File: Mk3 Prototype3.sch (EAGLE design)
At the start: 150 parts, among them IC1 TPD3E001DRL, IC2 TPS62082, IC3 STM32F401V, IC4 BQ24092, IC6 CC3100MOD, IC7 BQ2970, IC8 LSM6DS3, IC9 LIS3MDL, J1 ZX62-AB-5PA(11), J2 ER-CON50HT-1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

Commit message: updating usd
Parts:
- U1: value USD-SOCKET-SDIODM3AT_0011 -> USD-SOCKET-SDIO; device TiLDA Mk3 Parts:USD-SOCKET-SDIODM3AT_0011 -> TiLDA Mk3 Parts:USD-SOCKET-SDIO
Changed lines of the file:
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@@
 <part name="GND14" library="TiLDA Mk3 Parts" deviceset="GND" device=""/>
 <part name="R24" library="TiLDA Mk3 Parts" deviceset="R-EU_" device="0603K-SMALL" value="0603/330/5%"/>
-<part name="U1" library="TiLDA Mk3 Parts" deviceset="USD-SOCKET-SDIO" device="DM3AT_0011">
+<part name="U1" library="TiLDA Mk3 Parts" deviceset="USD-SOCKET-SDIO" device="" value="USD-SOCKET-SDIO">
 <attribute name="FARNELL" value="2427719"/>
 </part>

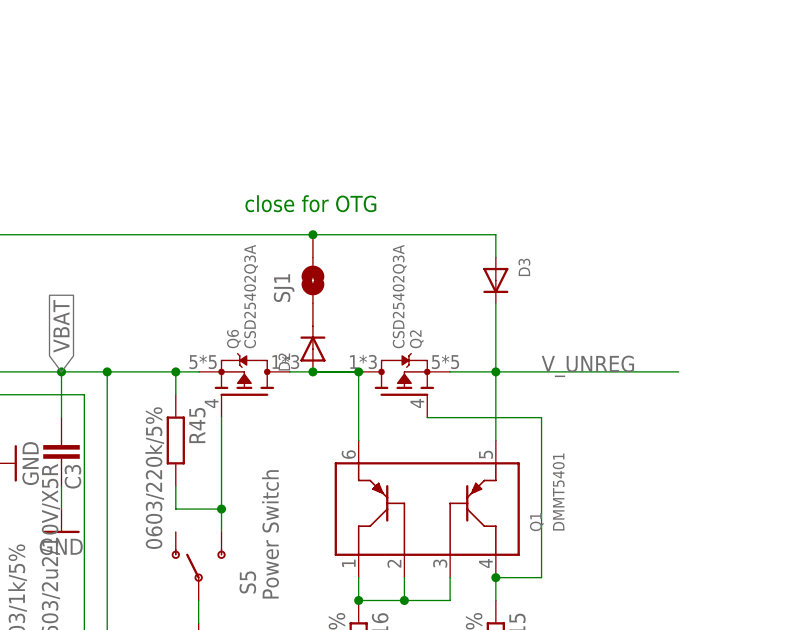
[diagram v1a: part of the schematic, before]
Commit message: changing out diodes
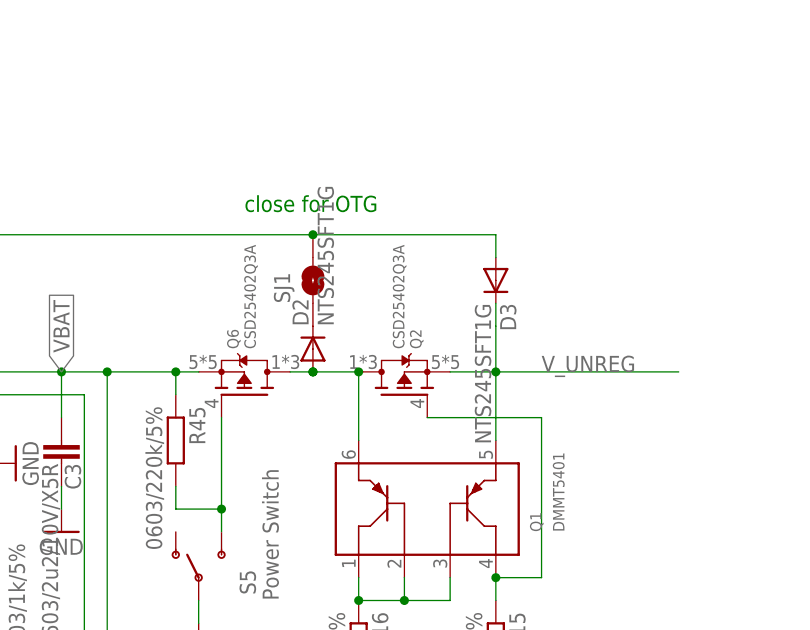
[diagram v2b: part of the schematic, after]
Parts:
- D2, D3: value (none) -> NTS245SFT1G; device TiLDA Mk3 Parts:DIODESOD-323F -> Diodes:1N4148-SOD123; FARNELL 1757770 -> (none)
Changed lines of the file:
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@@
 <part name="C6" library="passives-7351" deviceset="CAPACITOR" device="0805-N" value="0805/10u/10V/X5R"/>
 <part name="GND94" library="TiLDA Mk3 Parts" deviceset="GND" device=""/>
-<part name="D3" library="TiLDA Mk3 Parts" deviceset="DIODE" device="SOD-323F">
-<attribute name="FARNELL" value="1757770"/>
-</part>
-<part name="D2" library="TiLDA Mk3 Parts" deviceset="DIODE" device="SOD-323F">
-<attribute name="FARNELL" value="1757770"/>
-</part>
 <part name="SJ1" library="SparkFun-Passives" deviceset="JUMPER-PAD-2-NO" device="YES_SILK">
 <variant name="L4" populate="no"/>
@@
 <part name="FID2" library="TiLDA Mk3 Parts" deviceset="FIDUCIAL" device="1X2.5-STOP"/>
 <part name="FID5" library="TiLDA Mk3 Parts" deviceset="FIDUCIAL" device="1X2.5-STOP"/>
+<part name="D3" library="Diodes" deviceset="1N4148" device="-SOD123" value="NTS245SFT1G"/>
+<part name="D2" library="Diodes" deviceset="1N4148" device="-SOD123" value="NTS245SFT1G"/>
 </parts>
 <sheets>
@@
 </instance>
 <instance part="GND94" gate="1" x="576.58" y="185.42"/>
-<instance part="D3" gate="G$1" x="665.48" y="134.62" rot="R270">
-<attribute name="FARNELL" x="665.48" y="134.62" size="1.778" layer="96" rot="R270" display="off"/>
-</instance>
-<instance part="D2" gate="G$1" x="645.16" y="127" rot="R90">
-<attribute name="FARNELL" x="645.16" y="127" size="1.778" layer="96" rot="R90" display="off"/>
-</instance>
 <instance part="SJ1" gate="G$1" x="645.16" y="134.62" smashed="yes" rot="R90">
 <attribute name="NAME" x="642.62" y="132.08" size="1.778" layer="95" rot="R90"/>
@@
 <instance part="FID2" gate="G$1" x="370.84" y="22.86"/>
 <instance part="FID5" gate="G$1" x="375.92" y="22.86"/>
+<instance part="D3" gate="G$1" x="665.48" y="134.62" rot="R270"/>
+<instance part="D2" gate="G$1" x="645.16" y="127" rot="R90"/>
 </instances>
 <busses>
@@
 <junction x="665.48" y="124.46"/>
 <pinref part="D3" gate="G$1" pin="C"/>
-<wire x1="665.48" y1="132.08" x2="665.48" y2="124.46" width="0.1524" layer="91"/>
+<wire x1="665.48" y1="129.54" x2="665.48" y2="124.46" width="0.1524" layer="91"/>
+<wire x1="665.48" y1="132.08" x2="665.48" y2="129.54" width="0.1524" layer="91"/>
 </segment>
 <segment>
@@
 <segment>
 <junction x="546.1" y="124.46"/>
-<wire x1="665.48" y1="137.16" x2="665.48" y2="139.7" width="0.1524" layer="91"/>
 <wire x1="665.48" y1="139.7" x2="645.16" y2="139.7" width="0.1524" layer="91"/>
 <wire x1="645.16" y1="139.7" x2="546.1" y2="139.7" width="0.1524" layer="91"/>
@@
 <wire x1="546.1" y1="119.38" x2="546.1" y2="124.46" width="0.1524" layer="91"/>
 <junction x="546.1" y="119.38"/>
-<pinref part="D3" gate="G$1" pin="A"/>
 <pinref part="SJ1" gate="G$1" pin="2"/>
 <junction x="645.16" y="139.7"/>
+<pinref part="D3" gate="G$1" pin="A"/>
+<wire x1="665.48" y1="139.7" x2="665.48" y2="137.16" width="0.1524" layer="91"/>
 </segment>
 </net>
@@
 <pinref part="Q1" gate="G$1" pin="E1"/>
 <wire x1="650.24" y1="116.84" x2="650.24" y2="124.46" width="0.1524" layer="91"/>
-<wire x1="645.16" y1="124.46" x2="650.24" y2="124.46" width="0.1524" layer="91"/>
 <pinref part="Q6" gate="G$1" pin="D"/>
 <wire x1="650.24" y1="124.46" x2="645.16" y2="124.46" width="0.1524" layer="91"/>
 <junction x="650.24" y="124.46"/>
-<pinref part="D2" gate="G$1" pin="A"/>
 <wire x1="645.16" y1="124.46" x2="642.62" y2="124.46" width="0.1524" layer="91"/>
 <junction x="645.16" y="124.46"/>
+<pinref part="D2" gate="G$1" pin="A"/>
+<junction x="645.16" y="124.46"/>
 </segment>

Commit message: routing done
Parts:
- removed R24: 0603/330/5%, TiLDA Mk3 Parts:R-EU_0603K-SMALL
- added TP4: TPB1,27, TiLDA Mk3 Parts:TPB1,27
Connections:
- removed net SPI3_SCK: IC3_PB.PB3, J2.D/CX(SCL), R24.1
- net FSMC_A23: now also IC3_PB.PB3, J2.D/CX(SCL), TP4.TP; no longer R24.2
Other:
- note added: "/ SPI3_SCK"
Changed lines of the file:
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@@
 <part name="R13" library="TiLDA Mk3 Parts" deviceset="R-EU_" device="0603K-SMALL" value="0603/10k/5%"/>
 <part name="GND14" library="TiLDA Mk3 Parts" deviceset="GND" device=""/>
-<part name="R24" library="TiLDA Mk3 Parts" deviceset="R-EU_" device="0603K-SMALL" value="0603/330/5%"/>
 <part name="U1" library="TiLDA Mk3 Parts" deviceset="USD-SOCKET-SDIO" device="" value="USD-SOCKET-SDIO">
 <attribute name="FARNELL" value="2427719"/>
@@
 <part name="D3" library="Diodes" deviceset="1N4148" device="-SOD123" value="NTS245SFT1G"/>
 <part name="D2" library="Diodes" deviceset="1N4148" device="-SOD123" value="NTS245SFT1G"/>
+<part name="TP4" library="TiLDA Mk3 Parts" deviceset="TP" device="B1,27"/>
 </parts>
 <sheets>
@@
 <text x="322.58" y="228.6" size="1.778" layer="91">CH2,4: headers</text>
 <text x="322.58" y="220.98" size="1.778" layer="91">CH1: buzzer</text>
+<text x="83.82" y="195.58" size="1.778" layer="91">/ SPI3_SCK</text>
 </plain>
 <instances>
@@
 </instance>
 <instance part="GND14" gate="1" x="601.98" y="45.72"/>
-<instance part="R24" gate="G$1" x="728.98" y="139.7" rot="R180"/>
 <instance part="U1" gate="G$1" x="441.96" y="30.48">
 <attribute name="FARNELL" x="441.96" y="30.48" size="1.778" layer="96" display="off"/>
@@
 <instance part="D3" gate="G$1" x="665.48" y="134.62" rot="R270"/>
 <instance part="D2" gate="G$1" x="645.16" y="127" rot="R90"/>
+<instance part="TP4" gate="G$1" x="731.52" y="137.16" smashed="yes" rot="R180">
+<attribute name="NAME" x="732.79" y="135.89" size="1.778" layer="95" rot="R180"/>
+</instance>
 </instances>
 <busses>
@@
 </segment>
 </net>
-<net name="SPI3_SCK" class="0">
-<segment>
-<wire x1="68.58" y1="195.58" x2="71.12" y2="195.58" width="0.1524" layer="91"/>
-<label x="71.12" y="195.58" size="1.778" layer="95"/>
-<pinref part="IC3" gate="_PB" pin="PB3"/>
-</segment>
-<segment>
-<wire x1="754.38" y1="139.7" x2="734.06" y2="139.7" width="0.1524" layer="91"/>
-<label x="739.14" y="139.7" size="1.778" layer="95"/>
-<pinref part="J2" gate="G$1" pin="D/CX(SCL)"/>
-<pinref part="R24" gate="G$1" pin="1"/>
-</segment>
-</net>
 <net name="SPI3_MOSI" class="0">
 <segment>
@@
 <segment>
 <label x="708.66" y="139.7" size="1.778" layer="95"/>
-<wire x1="706.12" y1="139.7" x2="723.9" y2="139.7" width="0.1524" layer="91"/>
-<pinref part="R24" gate="G$1" pin="2"/>
-</segment>
-</net>
+<pinref part="J2" gate="G$1" pin="D/CX(SCL)"/>
+<wire x1="754.38" y1="139.7" x2="731.52" y2="139.7" width="0.1524" layer="91"/>
+<pinref part="TP4" gate="G$1" pin="TP"/>
+<wire x1="731.52" y1="139.7" x2="706.12" y2="139.7" width="0.1524" layer="91"/>
+<junction x="731.52" y="139.7"/>
+</segment>
+<segment>
+<wire x1="68.58" y1="195.58" x2="71.12" y2="195.58" width="0.1524" layer="91"/>
+<label x="71.12" y="195.58" size="1.778" layer="95"/>
+<pinref part="IC3" gate="_PB" pin="PB3"/>
+</segment>
+</net>

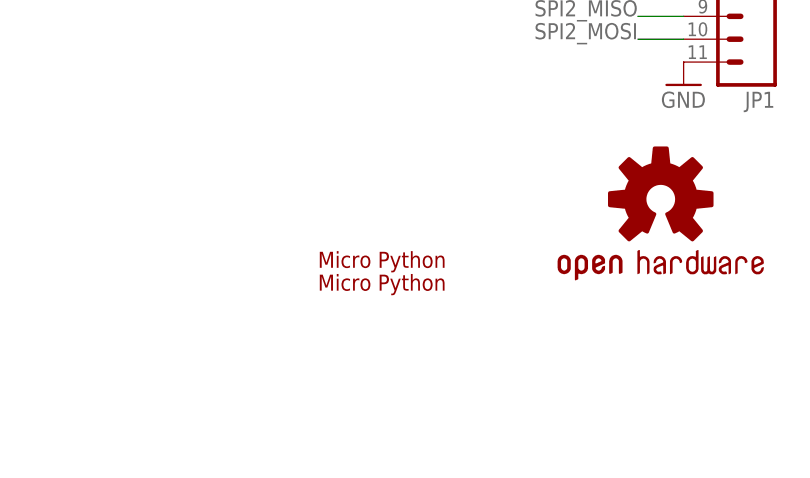
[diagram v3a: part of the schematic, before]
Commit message: some silk cleanup
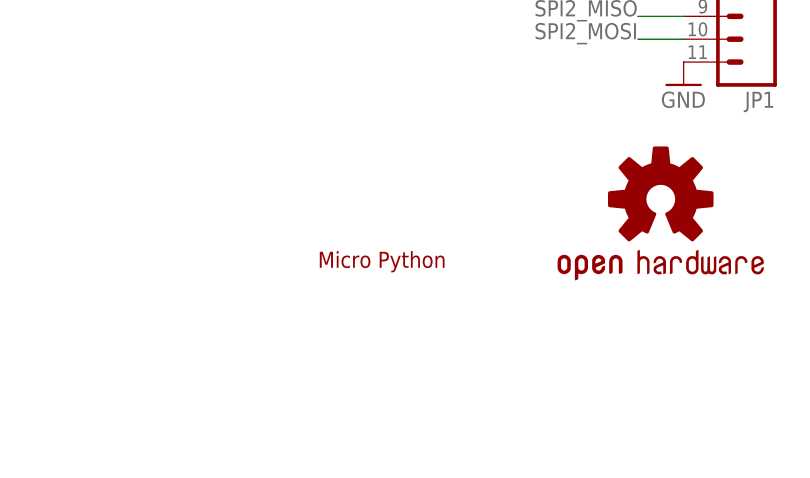
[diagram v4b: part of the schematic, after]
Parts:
- removed LOGO2: MICROPYTHON-SILK, TiLDA Mk3 Parts:MICROPYTHON-SILK
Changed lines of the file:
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@@
-<variant name="L4" populate="no"/>
-</part>
-<part name="LOGO2" library="TiLDA Mk3 Parts" deviceset="MICROPYTHON" device="-SILK">
 <variant name="L4" populate="no"/>
 </part>
@@
 <instance part="+3V21" gate="G$1" x="210.82" y="40.64" rot="R90"/>
 <instance part="OUTLINE1" gate="G$1" x="530.86" y="38.1"/>
-<instance part="LOGO2" gate="G$1" x="292.1" y="5.08"/>
 <instance part="LOGO3" gate="G$1" x="292.1" y="7.62"/>
 <instance part="U2" gate="G$1" x="767.08" y="88.9"/>

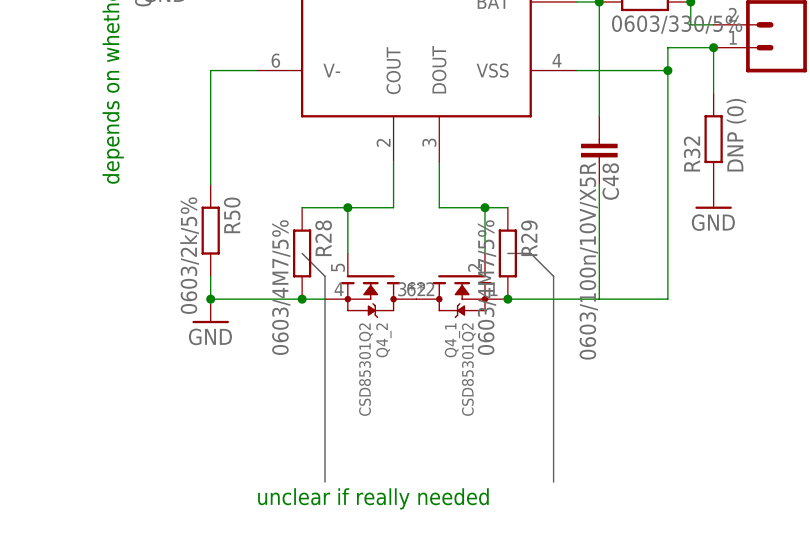
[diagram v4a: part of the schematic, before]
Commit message: Angle and clearance tidy
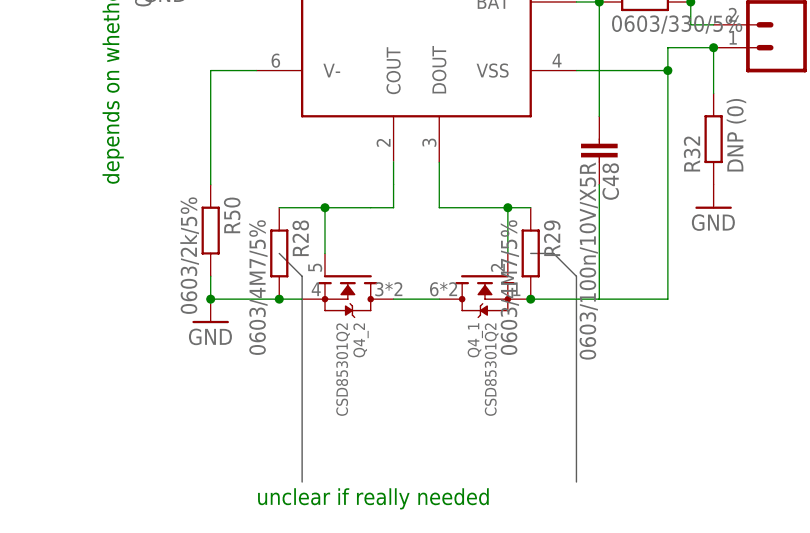
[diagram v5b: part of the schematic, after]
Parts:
- J3: value SWD_SHROUD -> SWD_SHROUD-PINHEAD; device dtb:SWD_SHROUD -> TiLDA Mk3 Parts:SWD_SHROUD-PINHEAD
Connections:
- net N$26 renamed SDX
- net N$29 renamed SCX
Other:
- moved on the sheet: Q4_1, Q4_2, R28, R29
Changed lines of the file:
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@@
 <part name="GND5" library="TiLDA Mk3 Parts" deviceset="GND" device=""/>
 <part name="FRAME2" library="TiLDA Mk3 Parts" deviceset="A3L-LOC" device=""/>
-<part name="J3" library="dtb" deviceset="SWD_SHROUD" device="" value="SWD_SHROUD">
+<part name="J3" library="TiLDA Mk3 Parts" deviceset="SWD_SHROUD" device="-PINHEAD" value="SWD_SHROUD-PINHEAD">
 <attribute name="FARNELL" value="1865285"/>
 </part>
@@
 <text x="406.4" y="198.12" size="1.778" layer="95" rot="R90">in theory the full 200u might not be needed</text>
 <text x="612.14" y="-12.7" size="1.778" layer="91">unclear if really needed</text>
-<wire x1="617.22" y1="15.24" x2="619.76" y2="12.7" width="0.1524" layer="97"/>
-<wire x1="619.76" y1="12.7" x2="619.76" y2="-10.16" width="0.1524" layer="97"/>
-<wire x1="640.08" y1="15.24" x2="642.62" y2="15.24" width="0.1524" layer="97"/>
-<wire x1="642.62" y1="15.24" x2="645.16" y2="12.7" width="0.1524" layer="97"/>
-<wire x1="645.16" y1="12.7" x2="645.16" y2="-10.16" width="0.1524" layer="97"/>
+<wire x1="614.68" y1="15.24" x2="617.22" y2="12.7" width="0.1524" layer="97"/>
+<wire x1="617.22" y1="12.7" x2="617.22" y2="-10.16" width="0.1524" layer="97"/>
+<wire x1="642.62" y1="15.24" x2="645.16" y2="15.24" width="0.1524" layer="97"/>
+<wire x1="645.16" y1="15.24" x2="647.7" y2="12.7" width="0.1524" layer="97"/>
+<wire x1="647.7" y1="12.7" x2="647.7" y2="-10.16" width="0.1524" layer="97"/>
 <text x="88.9" y="210.82" size="1.778" layer="97">check this for L4</text>
 <text x="210.82" y="91.44" size="1.778" layer="91" rot="R90">shouldnt be needed</text>
@@
 </instance>
 <instance part="GND9" gate="1" x="647.7" y="185.42"/>
-<instance part="Q4" gate="_1" x="635" y="12.7" rot="MR270"/>
-<instance part="Q4" gate="_2" x="624.84" y="12.7" rot="R270">
-<attribute name="FARNELL" x="624.84" y="12.7" size="1.778" layer="96" rot="R270" display="off"/>
+<instance part="Q4" gate="_1" x="637.54" y="12.7" rot="MR270"/>
+<instance part="Q4" gate="_2" x="622.3" y="12.7" rot="R270">
+<attribute name="FARNELL" x="622.3" y="12.7" size="1.778" layer="96" rot="R270" display="off"/>
 </instance>
 <instance part="IC4" gate="G$1" x="586.74" y="119.38">
@@
 <instance part="R19" gate="G$1" x="236.22" y="144.78" rot="R270"/>
 <instance part="+3V3" gate="G$1" x="236.22" y="152.4"/>
-<instance part="R28" gate="G$1" x="617.22" y="15.24" smashed="yes" rot="R270">
-<attribute name="NAME" x="618.7186" y="19.05" size="1.778" layer="95" rot="R270"/>
-<attribute name="VALUE" x="613.918" y="19.05" size="1.778" layer="96" rot="R270"/>
-<attribute name="FARNELL" x="617.22" y="15.24" size="1.778" layer="96" rot="R270" display="off"/>
-</instance>
-<instance part="R29" gate="G$1" x="640.08" y="15.24" smashed="yes" rot="R270">
-<attribute name="NAME" x="641.5786" y="19.05" size="1.778" layer="95" rot="R270"/>
-<attribute name="VALUE" x="636.778" y="19.05" size="1.778" layer="96" rot="R270"/>
-<attribute name="FARNELL" x="640.08" y="15.24" size="1.778" layer="96" rot="R270" display="off"/>
+<instance part="R28" gate="G$1" x="614.68" y="15.24" smashed="yes" rot="R270">
+<attribute name="NAME" x="616.1786" y="19.05" size="1.778" layer="95" rot="R270"/>
+<attribute name="VALUE" x="611.378" y="19.05" size="1.778" layer="96" rot="R270"/>
+<attribute name="FARNELL" x="614.68" y="15.24" size="1.778" layer="96" rot="R270" display="off"/>
+</instance>
+<instance part="R29" gate="G$1" x="642.62" y="15.24" smashed="yes" rot="R270">
+<attribute name="NAME" x="644.1186" y="19.05" size="1.778" layer="95" rot="R270"/>
+<attribute name="VALUE" x="639.318" y="19.05" size="1.778" layer="96" rot="R270"/>
+<attribute name="FARNELL" x="642.62" y="15.24" size="1.778" layer="96" rot="R270" display="off"/>
 </instance>
 <instance part="IC8" gate="G$1" x="254" y="91.44">
@@
 </segment>
 <segment>
-<wire x1="619.76" y1="10.16" x2="617.22" y2="10.16" width="0.1524" layer="91"/>
+<wire x1="617.22" y1="10.16" x2="614.68" y2="10.16" width="0.1524" layer="91"/>
 <pinref part="GND56" gate="1" pin="GND"/>
 <pinref part="R50" gate="G$1" pin="2"/>
-<wire x1="617.22" y1="10.16" x2="607.06" y2="10.16" width="0.1524" layer="91"/>
+<wire x1="614.68" y1="10.16" x2="607.06" y2="10.16" width="0.1524" layer="91"/>
 <wire x1="607.06" y1="12.7" x2="607.06" y2="10.16" width="0.1524" layer="91"/>
 <junction x="607.06" y="10.16"/>
 <pinref part="Q4" gate="_2" pin="S"/>
 <pinref part="R28" gate="G$1" pin="2"/>
-<junction x="617.22" y="10.16"/>
+<junction x="614.68" y="10.16"/>
 </segment>
 <segment>
@@
 <segment>
 <pinref part="IC7" gate="G$1" pin="COUT"/>
-<wire x1="627.38" y1="25.4" x2="627.38" y2="20.32" width="0.1524" layer="91"/>
-<wire x1="627.38" y1="20.32" x2="622.3" y2="20.32" width="0.1524" layer="91"/>
-<wire x1="622.3" y1="20.32" x2="622.3" y2="15.24" width="0.1524" layer="91"/>
+<wire x1="627.38" y1="25.4" x2="627.38" y2="22.86" width="0.1524" layer="91"/>
+<wire x1="627.38" y1="22.86" x2="627.38" y2="20.32" width="0.1524" layer="91"/>
+<wire x1="627.38" y1="20.32" x2="624.84" y2="20.32" width="0.1524" layer="91"/>
+<wire x1="624.84" y1="20.32" x2="619.76" y2="20.32" width="0.1524" layer="91"/>
+<wire x1="619.76" y1="20.32" x2="619.76" y2="15.24" width="0.1524" layer="91"/>
 <pinref part="Q4" gate="_2" pin="G"/>
 <pinref part="R28" gate="G$1" pin="1"/>
-<wire x1="617.22" y1="20.32" x2="622.3" y2="20.32" width="0.1524" layer="91"/>
-<junction x="622.3" y="20.32"/>
+<wire x1="614.68" y1="20.32" x2="619.76" y2="20.32" width="0.1524" layer="91"/>
+<junction x="619.76" y="20.32"/>
 </segment>
 </net>
@@
 <pinref part="IC7" gate="G$1" pin="DOUT"/>
 <wire x1="632.46" y1="25.4" x2="632.46" y2="20.32" width="0.1524" layer="91"/>
-<wire x1="632.46" y1="20.32" x2="637.54" y2="20.32" width="0.1524" layer="91"/>
-<wire x1="637.54" y1="20.32" x2="637.54" y2="15.24" width="0.1524" layer="91"/>
+<wire x1="632.46" y1="20.32" x2="640.08" y2="20.32" width="0.1524" layer="91"/>
+<wire x1="640.08" y1="20.32" x2="640.08" y2="15.24" width="0.1524" layer="91"/>
 <pinref part="Q4" gate="_1" pin="G"/>
 <pinref part="R29" gate="G$1" pin="1"/>
-<wire x1="637.54" y1="20.32" x2="640.08" y2="20.32" width="0.1524" layer="91"/>
-<junction x="637.54" y="20.32"/>
+<wire x1="640.08" y1="20.32" x2="642.62" y2="20.32" width="0.1524" layer="91"/>
+<junction x="640.08" y="20.32"/>
 </segment>
 </net>
@@
 <wire x1="657.86" y1="10.16" x2="650.24" y2="10.16" width="0.1524" layer="91"/>
 <pinref part="IC7" gate="G$1" pin="VSS"/>
-<wire x1="650.24" y1="10.16" x2="640.08" y2="10.16" width="0.1524" layer="91"/>
+<wire x1="650.24" y1="10.16" x2="642.62" y2="10.16" width="0.1524" layer="91"/>
 <wire x1="647.7" y1="35.56" x2="657.86" y2="35.56" width="0.1524" layer="91"/>
 <junction x="657.86" y="35.56"/>
@@
 <pinref part="Q4" gate="_1" pin="S"/>
 <pinref part="R29" gate="G$1" pin="2"/>
-<junction x="640.08" y="10.16"/>
+<junction x="642.62" y="10.16"/>
 <pinref part="R32" gate="G$1" pin="2"/>
 <wire x1="662.94" y1="33.02" x2="662.94" y2="38.1" width="0.1524" layer="91"/>
@@
 <pinref part="Q4" gate="_2" pin="D"/>
 <pinref part="Q4" gate="_1" pin="D"/>
+<wire x1="627.38" y1="10.16" x2="632.46" y2="10.16" width="0.1524" layer="91"/>
 </segment>
 </net>
@@
 </segment>
 </net>
-<net name="N$26" class="0">
+<net name="SDX" class="0">
 <segment>
 <pinref part="IC8" gate="G$1" pin="SDX"/>
@@
 </segment>
 </net>
-<net name="N$29" class="0">
+<net name="SCX" class="0">
 <segment>
 <pinref part="IC9" gate="G$1" pin="SCL/SPC"/>
